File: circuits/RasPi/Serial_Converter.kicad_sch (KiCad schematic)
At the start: 11 parts, among them J15 USB_C_Receptacle_USB2.0, U20 FT231XS

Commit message: 更新
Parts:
- removed J15: USB_C_Receptacle_USB2.0, Connector_USB:USB_C_Receptacle_G-Switch_GT-USB-7010ASV, symbol Connector:USB_C_Receptacle_USB2.0
- removed U20: FT231XS, Package_SO:SSOP-20_3.9x8.7mm_P0.635mm, symbol Interface_USB:FT231XS
- added J10: USB_C_Receptacle_USB2.0_16P, Connector_USB:USB_C_Receptacle_G-Switch_GT-USB-7010ASV, symbol Connector:USB_C_Receptacle_USB2.0_16P
- added U6: FT231XS, Package_SO:SSOP-20_3.9x8.7mm_P0.635mm, symbol Interface_USB:FT231XS
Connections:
- net GNDD: now also U6.16 (GND); no longer C58.2, C59.2, C60.1, R51.1, R52.1
- net MainRX_FT231X_TX: now also U6.20 (TXD)
- net MainTX_FT231X_RX: now also U6.4 (RXD)
- net VBUS: now also J10.A4 (VBUS), J10.A9 (VBUS), J10.B4 (VBUS), J10.B9 (VBUS), U6.15 (VCC)
- net at C60.2: now also U6.13 (3V3OUT), U6.14 (~{RESET}), U6.3 (VCCIO)
- net at R52.2: now also J10.A5 (CC1)
- net at C58.1, R115.2: now also J10.A7 (D-), J10.B7 (D-)
- net at R51.2: now also J10.B5 (CC2)
- net at C59.1, R101.2: now also J10.A6 (D+), J10.B6 (D+)
- net at R101.1: now also U6.11 (USBDP)
- net at R115.1: now also U6.12 (USBDM)
- new net: C58.2, C59.2, C60.1, J10.A1 (GND), J10.A12 (GND), J10.B1 (GND), J10.B12 (GND), J10.S1 (SHIELD), R51.1, R52.1, U6.6 (GND)
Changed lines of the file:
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@@
 (kicad_sch (version 20230121) (generator eeschema)
   (paper "A4")
+  (junction (at 109.22 66.04) (diameter 0) (color 0 0 0 0)
+  )
+  (junction (at 109.22 99.06) (diameter 0) (color 0 0 0 0)
+  )
+  (junction (at 96.52 99.06) (diameter 0) (color 0 0 0 0)
+  )
+  (junction (at 93.98 68.58) (diameter 0) (color 0 0 0 0)
+  )
+  (junction (at 104.14 99.06) (diameter 0) (color 0 0 0 0)
+  )
+  (junction (at 119.38 78.74) (diameter 0) (color 0 0 0 0)
+  )
+  (junction (at 104.14 68.58) (diameter 0) (color 0 0 0 0)
+  )
+  (junction (at 119.38 99.06) (diameter 0) (color 0 0 0 0)
+  )
+  (junction (at 134.62 53.34) (diameter 0) (color 0 0 0 0)
+  )
+  (junction (at 96.52 53.34) (diameter 0) (color 0 0 0 0)
+  )
+  (junction (at 93.98 99.06) (diameter 0) (color 0 0 0 0)
+  )
   (junction (at 93.98 66.04) (diameter 0) (color 0 0 0 0)
   )
-  (junction (at 109.22 66.04) (diameter 0) (color 0 0 0 0)
-  )
-  (junction (at 109.22 99.06) (diameter 0) (color 0 0 0 0)
-  )
-  (junction (at 93.98 68.58) (diameter 0) (color 0 0 0 0)
-  )
-  (junction (at 96.52 99.06) (diameter 0) (color 0 0 0 0)
+  (junction (at 78.74 99.06) (diameter 0) (color 0 0 0 0)
   )
   (junction (at 119.38 86.36) (diameter 0) (color 0 0 0 0)
   )
-  (junction (at 104.14 99.06) (diameter 0) (color 0 0 0 0)
-  )
-  (junction (at 104.14 68.58) (diameter 0) (color 0 0 0 0)
-  )
-  (junction (at 139.7 99.06) (diameter 0) (color 0 0 0 0)
-  )
-  (junction (at 119.38 99.06) (diameter 0) (color 0 0 0 0)
-  )
-  (junction (at 96.52 53.34) (diameter 0) (color 0 0 0 0)
-  )
-  (junction (at 134.62 99.06) (diameter 0) (color 0 0 0 0)
-  )
-  (junction (at 93.98 99.06) (diameter 0) (color 0 0 0 0)
-  )
-  (junction (at 134.62 53.34) (diameter 0) (color 0 0 0 0)
-  )
-  (junction (at 78.74 99.06) (diameter 0) (color 0 0 0 0)
-  )
   (junction (at 99.06 53.34) (diameter 0) (color 0 0 0 0)
-  )
-  (junction (at 119.38 78.74) (diameter 0) (color 0 0 0 0)
   )
   (no_connect (at 154.94 91.44))
@@
   (no_connect (at 154.94 86.36))
   (no_connect (at 154.94 73.66))
-  (wire (pts (xy 134.62 53.34) (xy 138.43 53.34))
-    (stroke (width 0) (type default))
-  )
   (wire (pts (xy 119.38 78.74) (xy 119.38 86.36))
+    (stroke (width 0) (type default))
+  )
+  (wire (pts (xy 119.38 76.2) (xy 119.38 78.74))
     (stroke (width 0) (type default))
   )
@@
     (stroke (width 0.5) (type solid))
   )
-  (wire (pts (xy 119.38 76.2) (xy 119.38 78.74))
-    (stroke (width 0) (type default))
-  )
-  (wire (pts (xy 139.7 99.06) (xy 134.62 99.06))
+  (wire (pts (xy 119.38 86.36) (xy 119.38 87.63))
+    (stroke (width 0) (type default))
+  )
+  (wire (pts (xy 104.14 68.58) (xy 110.49 68.58))
+    (stroke (width 0) (type default))
+  )
+  (wire (pts (xy 119.38 99.06) (xy 134.62 99.06))
+    (stroke (width 0) (type default))
+  )
+  (wire (pts (xy 93.98 63.5) (xy 93.98 66.04))
+    (stroke (width 0) (type default))
+  )
+  (wire (pts (xy 139.7 101.6) (xy 139.7 99.06))
+    (stroke (width 0) (type default))
+  )
+  (wire (pts (xy 96.52 73.66) (xy 96.52 85.09))
+    (stroke (width 0) (type default))
+  )
+  (wire (pts (xy 119.38 66.04) (xy 118.11 66.04))
+    (stroke (width 0) (type default))
+  )
+  (wire (pts (xy 96.52 99.06) (xy 104.14 99.06))
+    (stroke (width 0) (type default))
+  )
+  (wire (pts (xy 96.52 53.34) (xy 96.52 58.42))
+    (stroke (width 0) (type default))
+  )
+  (wire (pts (xy 157.48 63.5) (xy 154.94 63.5))
+    (stroke (width 0) (type default))
+  )
+  (wire (pts (xy 109.22 66.04) (xy 110.49 66.04))
+    (stroke (width 0) (type default))
+  )
+  (wire (pts (xy 104.14 80.01) (xy 104.14 99.06))
+    (stroke (width 0) (type default))
+  )
+  (wire (pts (xy 99.06 50.8) (xy 99.06 53.34))
+    (stroke (width 0) (type default))
+  )
+  (wire (pts (xy 78.74 88.9) (xy 78.74 99.06))
+    (stroke (width 0) (type default))
+  )
+  (wire (pts (xy 71.12 88.9) (xy 71.12 99.06))
     (stroke (width 0) (type default))
   )
   (wire (pts (xy 93.98 76.2) (xy 93.98 85.09))
-    (stroke (width 0) (type default))
-  )
-  (wire (pts (xy 104.14 68.58) (xy 110.49 68.58))
-    (stroke (width 0) (type default))
-  )
-  (wire (pts (xy 134.62 99.06) (xy 119.38 99.06))
-    (stroke (width 0) (type default))
-  )
-  (wire (pts (xy 93.98 63.5) (xy 93.98 66.04))
-    (stroke (width 0) (type default))
-  )
-  (wire (pts (xy 139.7 101.6) (xy 139.7 99.06))
-    (stroke (width 0) (type default))
-  )
-  (wire (pts (xy 96.52 73.66) (xy 96.52 85.09))
-    (stroke (width 0) (type default))
-  )
-  (wire (pts (xy 119.38 66.04) (xy 118.11 66.04))
-    (stroke (width 0) (type default))
-  )
-  (wire (pts (xy 96.52 99.06) (xy 104.14 99.06))
-    (stroke (width 0) (type default))
-  )
-  (wire (pts (xy 96.52 53.34) (xy 96.52 58.42))
-    (stroke (width 0) (type default))
-  )
-  (wire (pts (xy 157.48 63.5) (xy 154.94 63.5))
-    (stroke (width 0) (type default))
-  )
-  (wire (pts (xy 109.22 66.04) (xy 110.49 66.04))
-    (stroke (width 0) (type default))
-  )
-  (wire (pts (xy 104.14 80.01) (xy 104.14 99.06))
-    (stroke (width 0) (type default))
-  )
-  (wire (pts (xy 99.06 50.8) (xy 99.06 53.34))
-    (stroke (width 0) (type default))
-  )
-  (wire (pts (xy 78.74 88.9) (xy 78.74 99.06))
-    (stroke (width 0) (type default))
-  )
-  (wire (pts (xy 71.12 88.9) (xy 71.12 99.06))
     (stroke (width 0) (type default))
   )
@@
     (stroke (width 0) (type default))
   )
+  (wire (pts (xy 134.62 53.34) (xy 138.43 53.34))
+    (stroke (width 0) (type default))
+  )
   (wire (pts (xy 93.98 66.04) (xy 109.22 66.04))
     (stroke (width 0) (type default))
@@
     (stroke (width 0.5) (type solid))
   )
-  (wire (pts (xy 119.38 86.36) (xy 119.38 87.63))
-    (stroke (width 0) (type default))
-  )
   (wire (pts (xy 104.14 99.06) (xy 109.22 99.06))
     (stroke (width 0) (type default))
@@
     )
   )
-  (symbol (lib_id "Connector:USB_C_Receptacle_USB2.0") (at 78.74 66.04 0) (unit 1)
-    (in_bom yes) (on_board yes) (dnp no) (fields_autoplaced)
-    (property "Reference" "J15" (at 78.74 43.18 0)
-      (effects (font (size 1.27 1.27)))
-    )
-    (property "Value" "USB_C_Receptacle_USB2.0" (at 78.74 45.72 0)
-      (effects (font (size 1.27 1.27)))
-    )
-    (property "Footprint" "Connector_USB:USB_C_Receptacle_G-Switch_GT-USB-7010ASV" (at 82.55 66.04 0)
-      (effects (font (size 1.27 1.27)) hide)
-    )
-    (property "Datasheet" "https://www.usb.org/sites/default/files/documents/usb_type-c.zip" (at 82.55 66.04 0)
-      (effects (font (size 1.27 1.27)) hide)
-    )
-    (pin "A1")
-    (pin "A12")
-    (pin "A4")
-    (pin "A5")
-    (pin "A6")
-    (pin "A7")
-    (pin "A8")
-    (pin "A9")
-    (pin "B1")
-    (pin "B12")
-    (pin "B4")
-    (pin "B5")
-    (pin "B6")
-    (pin "B7")
-    (pin "B8")
-    (pin "B9")
-    (pin "S1")
-    (instances
-      (project "RasPi"
-        (path "/689a9e74-f202-4ea4-bfbb-4341f2549250/fddad0c3-2af8-46e3-8794-fa1122d24d51/43daae10-1159-44a4-b6d7-7cc0f30c7fe6"
-          (reference "J15") (unit 1)
-        )
-      )
-    )
-  )
   (symbol (lib_id "power:GNDD") (at 149.86 53.34 0) (unit 1)
     (in_bom yes) (on_board yes) (dnp no)
@@
   (symbol (lib_id "Interface_USB:FT231XS") (at 137.16 76.2 0) (unit 1)
     (in_bom yes) (on_board yes) (dnp no)
-    (property "Reference" "U20" (at 147.32 99.06 0)
+    (property "Reference" "U6" (at 147.32 99.06 0)
       (effects (font (size 1.27 1.27)) (justify left))
     )
@@
       (project "RasPi"
         (path "/689a9e74-f202-4ea4-bfbb-4341f2549250/fddad0c3-2af8-46e3-8794-fa1122d24d51/43daae10-1159-44a4-b6d7-7cc0f30c7fe6"
-          (reference "U20") (unit 1)
+          (reference "U6") (unit 1)
         )
       )
@@
         )
       )
+    )
+  )
+  (symbol (lib_id "Connector:USB_C_Receptacle_USB2.0_16P") (at 78.74 66.04 0) (unit 1)
+    (in_bom yes) (on_board yes) (dnp no) (fields_autoplaced)
+    (property "Reference" "J10" (at 78.74 43.18 0)
+      (effects (font (size 1.27 1.27)))
+    )
+    (property "Value" "USB_C_Receptacle_USB2.0_16P" (at 78.74 45.72 0)
+      (effects (font (size 1.27 1.27)))
+    )
+    (property "Footprint" "Connector_USB:USB_C_Receptacle_G-Switch_GT-USB-7010ASV" (at 82.55 66.04 0)
+      (effects (font (size 1.27 1.27)) hide)
+    )
+    (property "Datasheet" "https://www.usb.org/sites/default/files/documents/usb_type-c.zip" (at 82.55 66.04 0)
+      (effects (font (size 1.27 1.27)) hide)
+    )
+    (pin "B9")
+    (pin "B5")
+    (pin "A6")
+    (pin "A7")
+    (pin "B12")
+    (pin "B6")
+    (pin "A9")
+    (pin "B8")
+    (pin "B7")
+    (pin "A5")
+    (pin "A8")
+    (pin "B4")
+    (pin "B1")
+    (pin "A1")
+    (pin "A12")
+    (pin "A4")
+    (pin "S1")
+    (instances
+      (project "RasPi"
+        (path "/689a9e74-f202-4ea4-bfbb-4341f2549250/fddad0c3-2af8-46e3-8794-fa1122d24d51/43daae10-1159-44a4-b6d7-7cc0f30c7fe6"
+          (reference "J10") (unit 1)
+        )
+      )

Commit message: raspi基板回路図
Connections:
- net GNDD: now also C58.2, C59.2, C60.1, J10.A1 (GND), J10.A12 (GND), J10.B1 (GND), J10.B12 (GND), J10.S1 (SHIELD), R51.1, R52.1, U6.6 (GND)
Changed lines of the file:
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@@
   (junction (at 104.14 99.06) (diameter 0) (color 0 0 0 0)
+  )
+  (junction (at 139.7 99.06) (diameter 0) (color 0 0 0 0)
   )
   (junction (at 119.38 78.74) (diameter 0) (color 0 0 0 0)
@@
   )
   (junction (at 134.62 53.34) (diameter 0) (color 0 0 0 0)
+  )
+  (junction (at 134.62 99.06) (diameter 0) (color 0 0 0 0)
   )
   (junction (at 96.52 53.34) (diameter 0) (color 0 0 0 0)
@@
     (stroke (width 0) (type default))
   )
+  (wire (pts (xy 134.62 99.06) (xy 139.7 99.06))
+    (stroke (width 0) (type default))
+  )

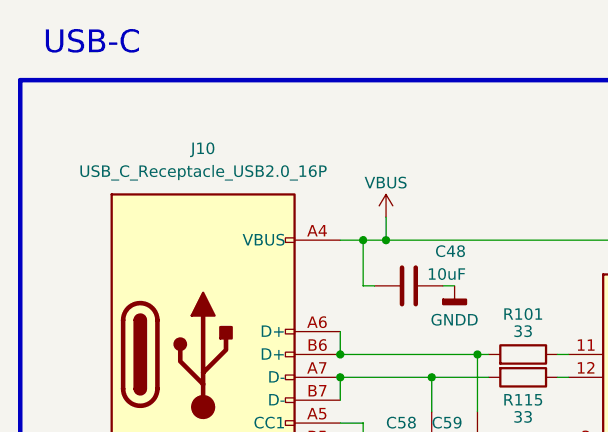
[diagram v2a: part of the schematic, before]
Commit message: 発注第2弾
RasPi発注
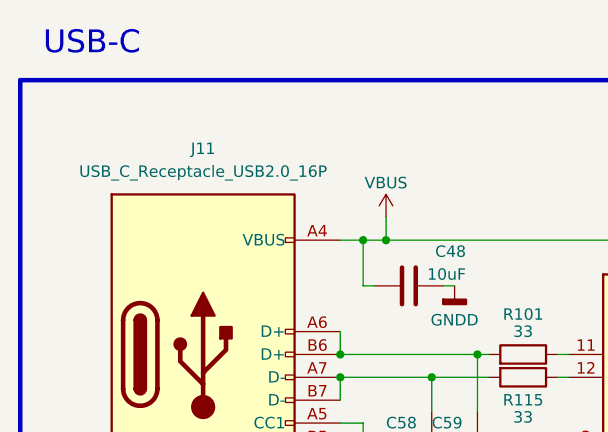
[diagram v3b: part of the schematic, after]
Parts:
- renumbered J10 to J11
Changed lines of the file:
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@@
   (symbol (lib_id "Connector:USB_C_Receptacle_USB2.0_16P") (at 78.74 66.04 0) (unit 1)
     (in_bom yes) (on_board yes) (dnp no) (fields_autoplaced)
-    (property "Reference" "J10" (at 78.74 43.18 0)
+    (property "Reference" "J11" (at 78.74 43.18 0)
       (effects (font (size 1.27 1.27)))
     )
@@
       (project "RasPi"
         (path "/689a9e74-f202-4ea4-bfbb-4341f2549250/fddad0c3-2af8-46e3-8794-fa1122d24d51/43daae10-1159-44a4-b6d7-7cc0f30c7fe6"
-          (reference "J10") (unit 1)
+          (reference "J11") (unit 1)
         )
       )
